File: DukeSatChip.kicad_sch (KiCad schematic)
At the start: 7 parts, among them J1 Conn_01x02_Pin

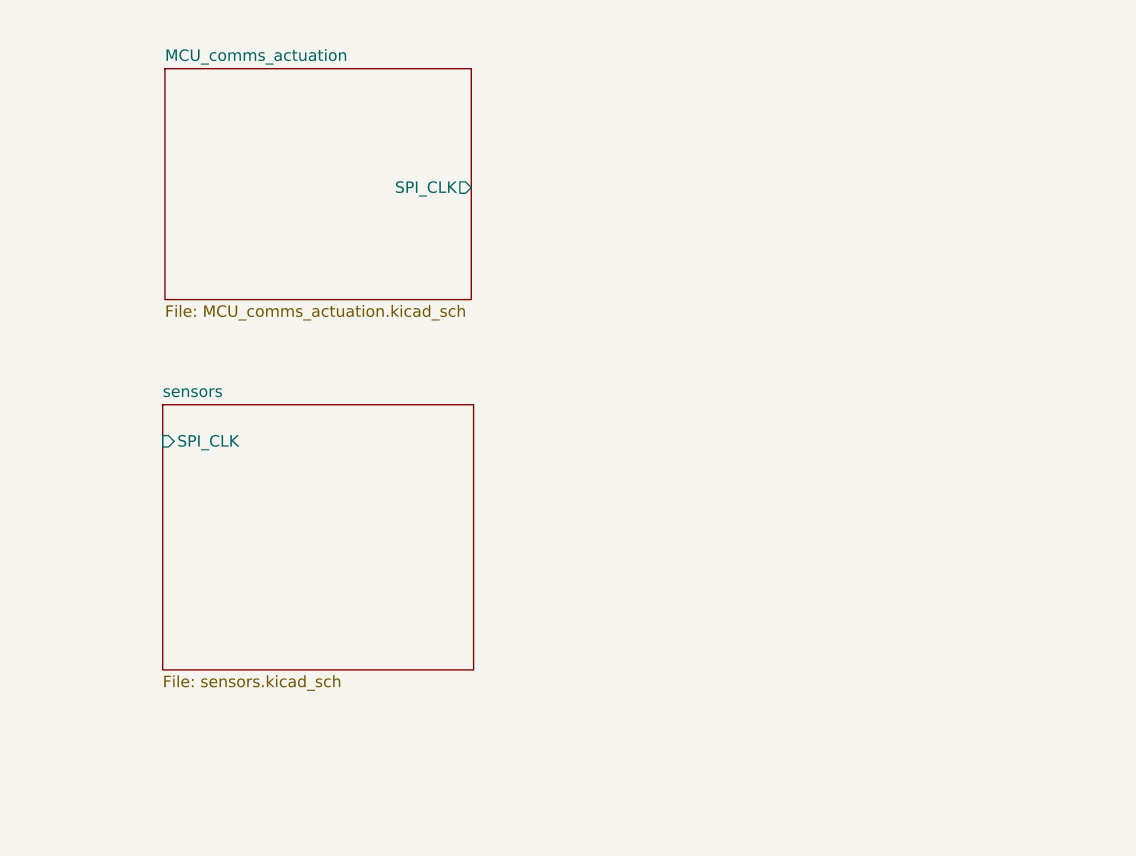
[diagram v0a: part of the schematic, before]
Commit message: Complete STM32 subsystem integration and schematic review
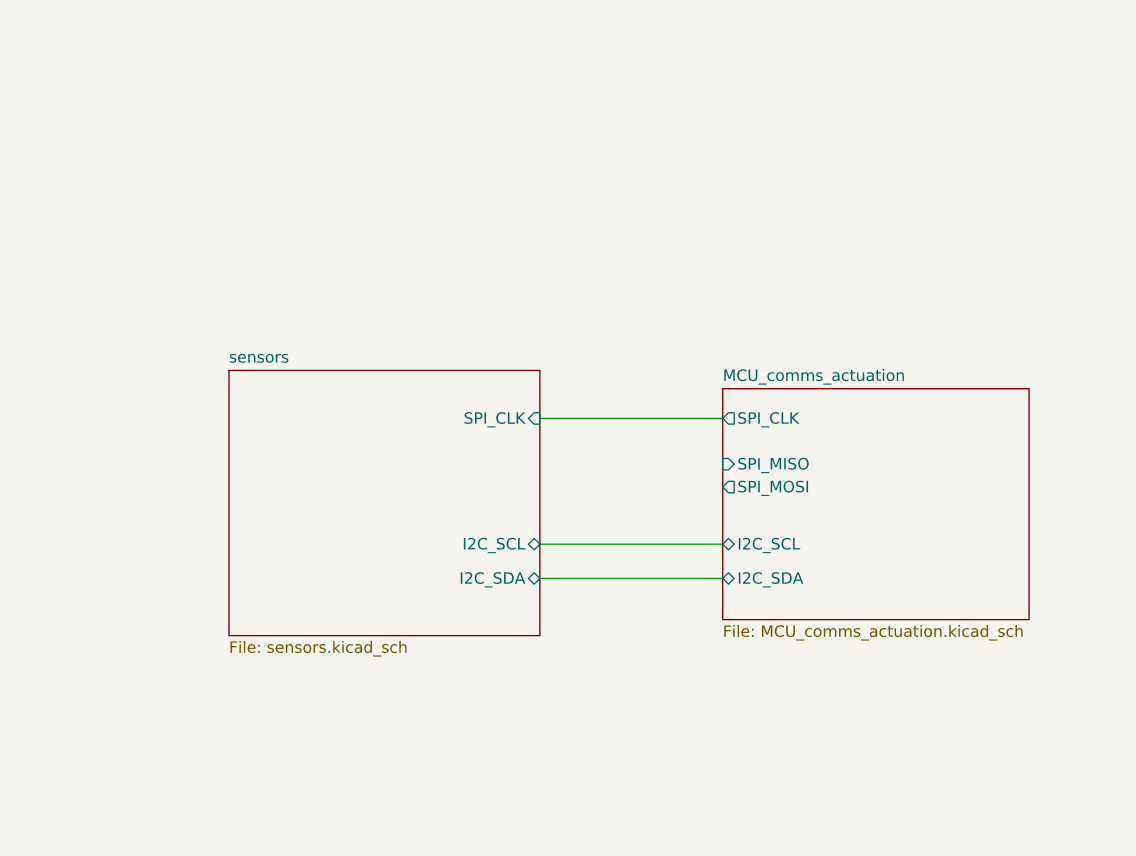
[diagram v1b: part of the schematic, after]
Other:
- sheet MCU_comms_actuation ports: added I2C_SCL, I2C_SDA, SPI_MISO, SPI_MOSI; removed none
- sheet sensors ports: added I2C_SCL, I2C_SDA; removed none
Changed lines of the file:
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@@
+	(wire
+		(pts
+			(xy 175.26 73.66) (xy 195.58 73.66)
+		)
+		(stroke
+			(width 0)
+			(type default)
+		)
+	)
 	(wire
 		(pts
@@
 	(wire
 		(pts
+			(xy 175.26 87.63) (xy 195.58 87.63)
+		)
+		(stroke
+			(width 0)
+			(type default)
+		)
+	)
+	(wire
+		(pts
 			(xy 69.85 58.42) (xy 67.31 58.42)
 		)
@@
 		(pts
 			(xy 38.1 66.04) (xy 48.26 66.04)
+		)
+		(stroke
+			(width 0)
+			(type default)
+		)
+	)
+	(wire
+		(pts
+			(xy 175.26 91.44) (xy 195.58 91.44)
 		)
 		(stroke
@@
 	)
 	(sheet
-		(at 133.604 34.798)
+		(at 195.58 70.358)
 		(size 34.036 25.654)
 		(exclude_from_sim no)
@@
 		)
 		(property "Sheetname" "MCU_comms_actuation"
-			(at 133.604 34.0864 0)
+			(at 195.58 69.6464 0)
 			(show_name no)
 			(do_not_autoplace no)
@@
 		)
 		(property "Sheetfile" "MCU_comms_actuation.kicad_sch"
-			(at 133.604 61.0366 0)
+			(at 195.58 96.5966 0)
 			(show_name no)
 			(do_not_autoplace no)
@@
 		)
 		(pin "SPI_CLK" output
-			(at 167.64 48.006 0)
-			(effects
-				(font
-					(size 1.27 1.27)
-				)
-				(justify right)
+			(at 195.58 73.66 180)
+			(effects
+				(font
+					(size 1.27 1.27)
+				)
+				(justify left)
+			)
+		)
+		(pin "SPI_MISO" input
+			(at 195.58 78.74 180)
+			(effects
+				(font
+					(size 1.27 1.27)
+				)
+				(justify left)
+			)
+		)
+		(pin "SPI_MOSI" output
+			(at 195.58 81.28 180)
+			(effects
+				(font
+					(size 1.27 1.27)
+				)
+				(justify left)
+			)
+		)
+		(pin "I2C_SCL" bidirectional
+			(at 195.58 87.63 180)
+			(effects
+				(font
+					(size 1.27 1.27)
+				)
+				(justify left)
+			)
+		)
+		(pin "I2C_SDA" bidirectional
+			(at 195.58 91.44 180)
+			(effects
+				(font
+					(size 1.27 1.27)
+				)
+				(justify left)
 			)
 		)
@@
 	)
 	(sheet
-		(at 133.35 72.136)
+		(at 140.716 68.326)
 		(size 34.544 29.464)
 		(exclude_from_sim no)
@@
 		)
 		(property "Sheetname" "sensors"
-			(at 133.35 71.4244 0)
+			(at 140.716 67.6144 0)
 			(show_name no)
 			(do_not_autoplace no)
@@
 		)
 		(property "Sheetfile" "sensors.kicad_sch"
-			(at 133.35 102.1846 0)
+			(at 140.716 98.3746 0)
 			(show_name no)
 			(do_not_autoplace no)
@@
 		)
 		(pin "SPI_CLK" input
-			(at 133.35 76.2 180)
-			(effects
-				(font
-					(size 1.27 1.27)
-				)
-				(justify left)
-			)
-		)
+			(at 175.26 73.66 0)
+			(effects
+				(font
+					(size 1.27 1.27)
+				)
+				(justify right)
+			)
+		)
+		(pin "I2C_SCL" bidirectional
+			(at 175.26 87.63 0)
+			(effects
+				(font
+					(size 1.27 1.27)
+				)
+				(justify right)
+			)
+		)
+		(pin "I2C_SDA" bidirectional
+			(at 175.26 91.44 0)
+			(effects
+				(font
+					(size 1.27 1.27)
+				)
+				(justify right)
+			)
+		)

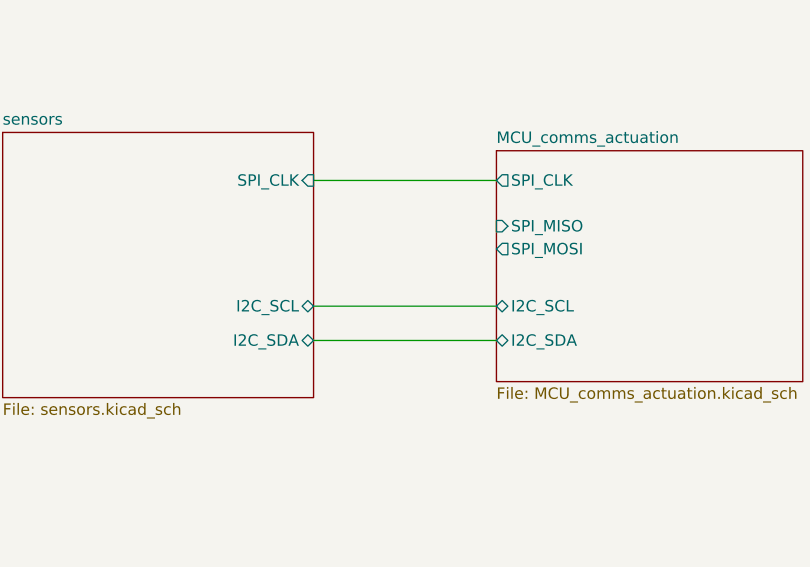
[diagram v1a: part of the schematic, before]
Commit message: Updated GPS, BMI, LSM, and BNO on sensors. Added hierachical labels and new "golden rule" connections
Updated each sensor ensuring they followed the golden rule. I also added hiearchical labels to the topsheet and the inside sheets. Fixed specific sensors to be in SPI vs I2C mode and updated the names.
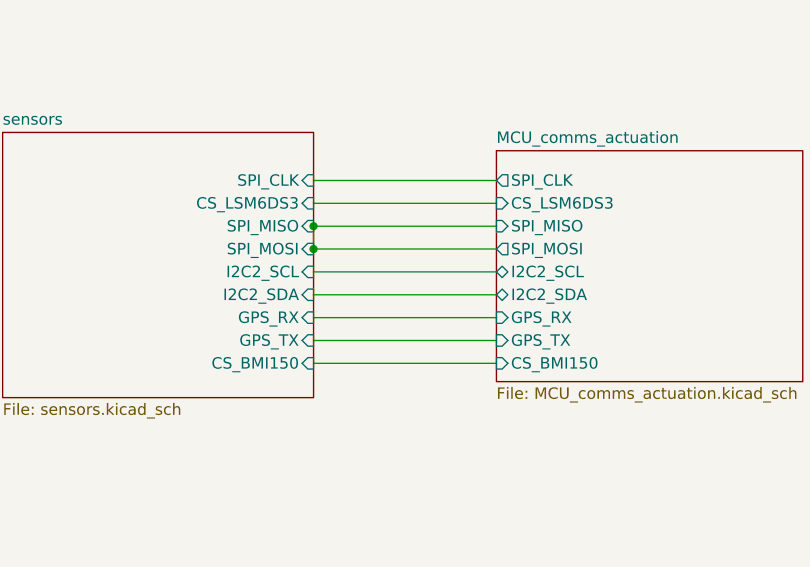
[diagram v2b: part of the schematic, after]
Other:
- sheet MCU_comms_actuation ports: added CS_BMI150, CS_LSM6DS3, GPS_RX, GPS_TX, I2C2_SCL, I2C2_SDA; removed I2C_SCL, I2C_SDA
- sheet sensors ports: added CS_BMI150, CS_LSM6DS3, GPS_RX, GPS_TX, I2C2_SCL, I2C2_SDA, SPI_MISO, SPI_MOSI; removed I2C_SCL, I2C_SDA
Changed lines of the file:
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@@
+	)
+	(junction
+		(at 175.26 81.28)
+		(diameter 0)
+		(color 0 0 0 0)
 	)
 	(junction
@@
 	)
 	(junction
+		(at 175.26 78.74)
+		(diameter 0)
+		(color 0 0 0 0)
+	)
+	(junction
 		(at 48.26 66.04)
 		(diameter 0)
@@
 	(wire
 		(pts
+			(xy 175.26 81.28) (xy 195.58 81.28)
+		)
+		(stroke
+			(width 0)
+			(type default)
+		)
+	)
+	(wire
+		(pts
+			(xy 175.26 91.44) (xy 195.58 91.44)
+		)
+		(stroke
+			(width 0)
+			(type default)
+		)
+	)
+	(wire
+		(pts
 			(xy 67.31 55.88) (xy 67.31 53.34)
 		)
@@
 	(wire
 		(pts
+			(xy 175.26 93.98) (xy 195.58 93.98)
+		)
+		(stroke
+			(width 0)
+			(type default)
+		)
+	)
+	(wire
+		(pts
+			(xy 175.26 78.74) (xy 175.26 81.28)
+		)
+		(stroke
+			(width 0)
+			(type default)
+		)
+	)
+	(wire
+		(pts
 			(xy 96.52 50.8) (xy 104.14 50.8)
 		)
@@
 	(wire
 		(pts
+			(xy 175.26 76.2) (xy 195.58 76.2)
+		)
+		(stroke
+			(width 0)
+			(type default)
+		)
+	)
+	(wire
+		(pts
 			(xy 100.33 35.56) (xy 100.33 48.26)
 		)
@@
 	(wire
 		(pts
-			(xy 175.26 87.63) (xy 195.58 87.63)
+			(xy 175.26 83.82) (xy 195.58 83.82)
 		)
 		(stroke
@@
 	(wire
 		(pts
-			(xy 175.26 91.44) (xy 195.58 91.44)
+			(xy 175.26 86.36) (xy 195.58 86.36)
 		)
 		(stroke
@@
 	(wire
 		(pts
+			(xy 175.26 78.74) (xy 195.58 78.74)
+		)
+		(stroke
+			(width 0)
+			(type default)
+		)
+	)
+	(wire
+		(pts
 			(xy 66.04 60.96) (xy 69.85 60.96)
 		)
@@
 		(pts
 			(xy 80.01 77.47) (xy 80.01 80.01)
+		)
+		(stroke
+			(width 0)
+			(type default)
+		)
+	)
+	(wire
+		(pts
+			(xy 175.26 88.9) (xy 195.58 88.9)
 		)
 		(stroke
@@
 			)
 		)
+		(pin "SPI_MOSI" output
+			(at 195.58 81.28 180)
+			(effects
+				(font
+					(size 1.27 1.27)
+				)
+				(justify left)
+			)
+		)
+		(pin "I2C2_SCL" bidirectional
+			(at 195.58 83.82 180)
+			(effects
+				(font
+					(size 1.27 1.27)
+				)
+				(justify left)
+			)
+		)
+		(pin "I2C2_SDA" bidirectional
+			(at 195.58 86.36 180)
+			(effects
+				(font
+					(size 1.27 1.27)
+				)
+				(justify left)
+			)
+		)
+		(pin "GPS_RX" input
+			(at 195.58 88.9 180)
+			(effects
+				(font
+					(size 1.27 1.27)
+				)
+				(justify left)
+			)
+		)
+		(pin "GPS_TX" input
+			(at 195.58 91.44 180)
+			(effects
+				(font
+					(size 1.27 1.27)
+				)
+				(justify left)
+			)
+		)
 		(pin "SPI_MISO" input
 			(at 195.58 78.74 180)
@@
 			)
 		)
-		(pin "SPI_MOSI" output
-			(at 195.58 81.28 180)
+		(pin "CS_BMI150" input
+			(at 195.58 93.98 180)
 			(effects
 				(font
@@
 			)
 		)
-		(pin "I2C_SCL" bidirectional
-			(at 195.58 87.63 180)
-			(effects
-				(font
-					(size 1.27 1.27)
-				)
-				(justify left)
-			)
-		)
-		(pin "I2C_SDA" bidirectional
-			(at 195.58 91.44 180)
+		(pin "CS_LSM6DS3" input
+			(at 195.58 76.2 180)
 			(effects
 				(font
@@
 			)
 		)
-		(pin "I2C_SCL" bidirectional
-			(at 175.26 87.63 0)
+		(pin "I2C2_SCL" input
+			(at 175.26 83.82 0)
 			(effects
 				(font
@@
 			)
 		)
-		(pin "I2C_SDA" bidirectional
+		(pin "I2C2_SDA" input
+			(at 175.26 86.36 0)
+			(effects
+				(font
+					(size 1.27 1.27)
+				)
+				(justify right)
+			)
+		)
+		(pin "CS_BMI150" input
+			(at 175.26 93.98 0)
+			(effects
+				(font
+					(size 1.27 1.27)
+				)
+				(justify right)
+			)
+		)
+		(pin "GPS_RX" input
+			(at 175.26 88.9 0)
+			(effects
+				(font
+					(size 1.27 1.27)
+				)
+				(justify right)
+			)
+		)
+		(pin "GPS_TX" input
 			(at 175.26 91.44 0)
 			(effects
 				(font
+					(size 1.27 1.27)
+				)
+				(justify right)
+			)
+		)
+		(pin "SPI_MISO" input
+			(at 175.26 78.74 0)
+			(effects
+				(font
+					(size 1.27 1.27)
+				)
+				(justify right)
+			)
+		)
+		(pin "SPI_MOSI" input
+			(at 175.26 81.28 0)
+			(effects
+				(font
+					(size 1.27 1.27)
+				)
+				(justify right)
+			)
+		)
+		(pin "CS_LSM6DS3" input
+			(at 175.26 76.2 0)
+			(effects
+				(font

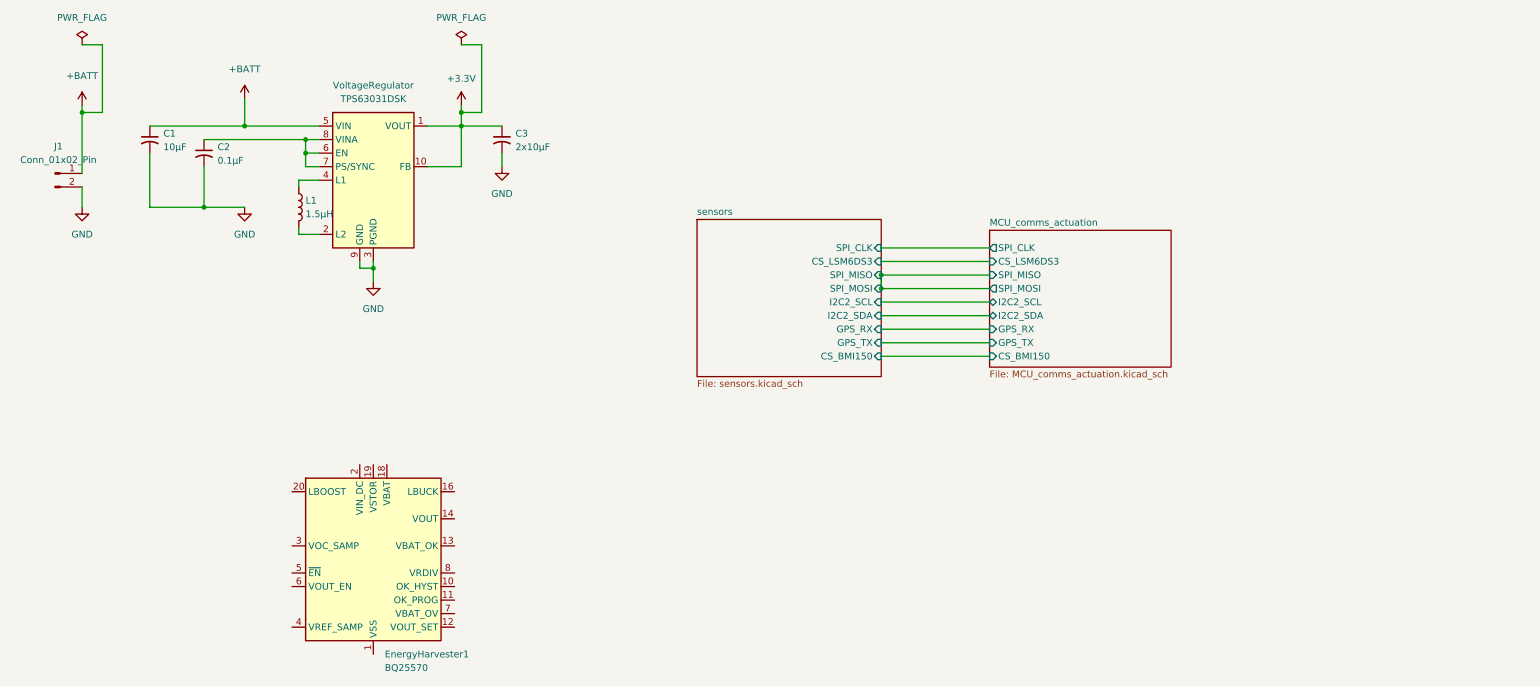
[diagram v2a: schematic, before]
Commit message: Add load switch for sleep rail and IMU interrupt
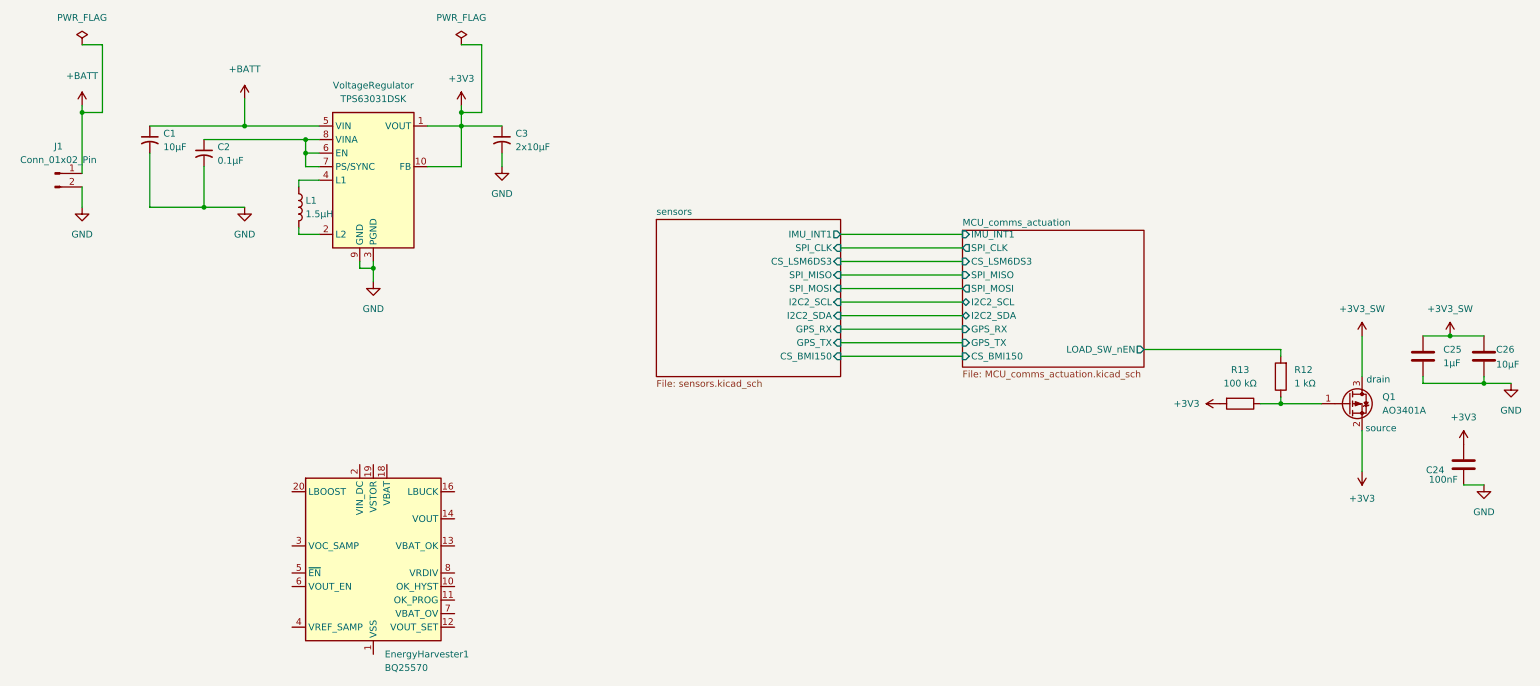
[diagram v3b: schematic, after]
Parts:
- added C24: 100nF, Capacitor_SMD:C_0603_1608Metric, symbol Device:C
- added C25: 1µF, Capacitor_SMD:C_0603_1608Metric, symbol Device:C
- added C26: 10µF, Capacitor_SMD:C_0805_2012Metric, symbol Device:C
- added Q1: AO3401A, Package_TO_SOT_SMD:SOT-23, symbol Transistor_FET:AO3401A
- added R12: 1 kΩ, symbol Device:R
- added R13: 100 kΩ, symbol Device:R
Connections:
- net GND: now also C24.2, C25.2, C26.2
- net +3.3V renamed +3V3
- net +3V3: now also C24.1, Q1.2 (S), R13.2
- new net: Q1.1 (G), R12.1, R13.1
- new net +3V3_SW: C25.1, C26.1, Q1.3 (D)
- new net MCU_comms_actuation/LOAD_SW_nEN: R12.2
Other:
- sheet MCU_comms_actuation ports: added IMU_INT1, LOAD_SW_nEN; removed none
- sheet sensors ports: added IMU_INT1; removed none
- note added: "drain"
- note added: "source"
